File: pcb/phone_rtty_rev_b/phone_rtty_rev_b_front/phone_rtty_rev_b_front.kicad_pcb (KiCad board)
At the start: 2 copper layers, 58 x 24 mm, 3 parts

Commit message: Minor changes.
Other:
- outline, holes or cut-outs redrawn
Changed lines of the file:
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@@
       (xy -2.537313 2.939947) (xy -2.454562 2.96715) (xy -2.376928 2.977424) (xy -2.273043 2.973429)) (layer B.Cu) (width 0.01))
   )
-  (gr_circle (center 133.5 111.7) (end 137 111.7) (layer Edge.Cuts) (width 0.15))
-  (gr_circle (center 143.7 111.7) (end 147.2 111.7) (layer Edge.Cuts) (width 0.15))
-  (gr_line (start 122.7 110.4) (end 122.7 117.2) (angle 90) (layer Dwgs.User) (width 0.05))
+  (gr_arc (start 143.7 111.7) (end 140.8 114.6) (angle 90) (layer F.SilkS) (width 0.35))
+  (gr_arc (start 143.7 111.7) (end 140.8 108.8) (angle 90) (layer F.SilkS) (width 0.35))
+  (gr_arc (start 143.7 111.7) (end 146.6 108.8) (angle 90) (layer F.SilkS) (width 0.35))
+  (gr_arc (start 133.5 111.7) (end 130.6 114.6) (angle 90) (layer F.SilkS) (width 0.35))
+  (gr_arc (start 133.5 111.7) (end 130.6 108.8) (angle 90) (layer F.SilkS) (width 0.35))
+  (gr_arc (start 133.5 111.7) (end 136.4 108.8) (angle 90) (layer F.SilkS) (width 0.35))
+  (gr_circle (center 122.7 114.2) (end 122.7 117.1) (layer Edge.Cuts) (width 0.15))
+  (gr_line (start 122.7 110.8) (end 122.7 117.6) (angle 90) (layer Dwgs.User) (width 0.05))
+  (gr_circle (center 133.5 111.7) (end 136.5 111.7) (layer Edge.Cuts) (width 0.15))
+  (gr_circle (center 143.7 111.7) (end 146.7 111.7) (layer Edge.Cuts) (width 0.15))
   (gr_line (start 140.5 108.5) (end 140.2 108.2) (angle 90) (layer F.SilkS) (width 0.35))
-  (gr_arc (start 143.7 111.7) (end 146.9 108.5) (angle 90) (layer F.SilkS) (width 0.35))
-  (gr_arc (start 143.7 111.7) (end 140.5 108.5) (angle 90) (layer F.SilkS) (width 0.35))
-  (gr_arc (start 143.7 111.7) (end 140.5 114.9) (angle 90) (layer F.SilkS) (width 0.35))
-  (gr_arc (start 133.5 111.7) (end 136.7 108.5) (angle 90) (layer F.SilkS) (width 0.35))
-  (gr_arc (start 133.5 111.7) (end 130.3 108.5) (angle 90) (layer F.SilkS) (width 0.35))
-  (gr_arc (start 133.5 111.7) (end 130.3 114.9) (angle 90) (layer F.SilkS) (width 0.35))
   (gr_line (start 147.2 115.2) (end 140.3 108.3) (angle 90) (layer Dwgs.User) (width 0.05))
   (gr_line (start 140.2 115.2) (end 147.2 108.2) (angle 90) (layer Dwgs.User) (width 0.05))
@@
   (gr_line (start 130 108.2) (end 130.3 108.5) (angle 90) (layer F.SilkS) (width 0.35))
   (gr_line (start 137 108.2) (end 136.7 108.5) (angle 90) (layer F.SilkS) (width 0.35))
-  (gr_line (start 128.5 111.7) (end 128.95 111.7) (angle 90) (layer F.SilkS) (width 0.35))
-  (gr_line (start 133.5 106.7) (end 133.5 107.15) (angle 90) (layer F.SilkS) (width 0.35))
-  (gr_line (start 118.8 113.8) (end 126.6 113.8) (angle 90) (layer Dwgs.User) (width 0.05))
+  (gr_line (start 128.55 111.7) (end 129 111.7) (angle 90) (layer F.SilkS) (width 0.35))
+  (gr_line (start 133.5 106.75) (end 133.5 107.2) (angle 90) (layer F.SilkS) (width 0.35))
+  (gr_line (start 118.8 114.2) (end 126.6 114.2) (angle 90) (layer Dwgs.User) (width 0.05))
   (gr_text "PCB level" (at 152.4 115.9) (layer Cmts.User)
     (effects (font (size 1.2 1.2) (thickness 0.1)))
@@
     (arrow2b (pts (xy 92 111.7) (xy 92.586421 112.826504)))
   )
-  (gr_line (start 138.05 111.7) (end 138.4 111.7) (angle 90) (layer F.SilkS) (width 0.35))
-  (gr_line (start 138.8 111.7) (end 139.15 111.7) (angle 90) (layer F.SilkS) (width 0.35))
-  (gr_line (start 148.25 111.7) (end 148.7 111.7) (angle 90) (layer F.SilkS) (width 0.35))
-  (gr_line (start 143.7 107.15) (end 143.7 106.7) (angle 90) (layer F.SilkS) (width 0.35))
+  (gr_line (start 138 111.7) (end 138.35 111.7) (angle 90) (layer F.SilkS) (width 0.35))
+  (gr_line (start 138.85 111.7) (end 139.2 111.7) (angle 90) (layer F.SilkS) (width 0.35))
+  (gr_line (start 148.2 111.7) (end 148.65 111.7) (angle 90) (layer F.SilkS) (width 0.35))
+  (gr_line (start 143.7 107.2) (end 143.7 106.75) (angle 90) (layer F.SilkS) (width 0.35))
   (gr_text PHONE (at 122.7 119.5) (layer F.SilkS)
     (effects (font (size 1.5 1.5) (thickness 0.3)))
@@
   (gr_line (start 133.5 106.7) (end 133.5 116.7) (angle 90) (layer Dwgs.User) (width 0.05))
   (gr_line (start 127.5 111.7) (end 149.7 111.7) (angle 90) (layer Dwgs.User) (width 0.05))
-  (gr_circle (center 122.7 113.8) (end 125.6 113.7) (layer Edge.Cuts) (width 0.15))
   (dimension 10.2 (width 0.1) (layer Dwgs.User)
     (gr_text "10.200 mm" (at 94.65 118.9 270) (layer Dwgs.User)

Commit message: Minor changes to revision B and gerbers.
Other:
- board text added: "RTTY Interface Rev. B Front Panel"
- board text removed: "RTTY Interface Revision B Front Panel"
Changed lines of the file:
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@@
     (links 0)
     (no_connects 0)
-    (area 99.924999 99.924999 158.075001 124.075001)
+    (area 81.883333 87.8 164.986666 136.700001)
     (thickness 1.6)
     (drawings 57)
@@
     (visible_elements 7FFFFFFF)
     (pcbplotparams
-      (layerselection 0x010f0_80000001)
+      (layerselection 0x010e0_80000001)
       (usegerberextensions true)
       (excludeedgelayer true)
@@
       (drillshape 0)
       (scaleselection 1)
-      (outputdirectory D:/MyProjects/phone_rtty_interface/gerbers))
+      (outputdirectory gerbers))
   )
   (net 0 "")
@@
       (xy -2.537313 2.939947) (xy -2.454562 2.96715) (xy -2.376928 2.977424) (xy -2.273043 2.973429)) (layer B.Cu) (width 0.01))
   )
+  (gr_line (start 147.8 111.7) (end 148.2 111.7) (angle 90) (layer F.SilkS) (width 0.35))
   (gr_arc (start 143.7 111.7) (end 140.8 114.6) (angle 90) (layer F.SilkS) (width 0.35))
   (gr_arc (start 143.7 111.7) (end 140.8 108.8) (angle 90) (layer F.SilkS) (width 0.35))
@@
   (gr_circle (center 133.5 111.7) (end 136.5 111.7) (layer Edge.Cuts) (width 0.15))
   (gr_circle (center 143.7 111.7) (end 146.7 111.7) (layer Edge.Cuts) (width 0.15))
-  (gr_line (start 140.5 108.5) (end 140.2 108.2) (angle 90) (layer F.SilkS) (width 0.35))
+  (gr_line (start 140.8 108.8) (end 140.5 108.5) (angle 90) (layer F.SilkS) (width 0.35))
   (gr_line (start 147.2 115.2) (end 140.3 108.3) (angle 90) (layer Dwgs.User) (width 0.05))
   (gr_line (start 140.2 115.2) (end 147.2 108.2) (angle 90) (layer Dwgs.User) (width 0.05))
   (gr_line (start 137 115.2) (end 130 108.2) (angle 90) (layer Dwgs.User) (width 0.05))
   (gr_line (start 130 115.2) (end 137 108.2) (angle 90) (layer Dwgs.User) (width 0.05))
-  (gr_line (start 147.2 115.2) (end 146.9 114.9) (angle 90) (layer F.SilkS) (width 0.35))
-  (gr_line (start 140.2 115.2) (end 140.5 114.9) (angle 90) (layer F.SilkS) (width 0.35))
-  (gr_line (start 147.2 108.2) (end 146.9 108.5) (angle 90) (layer F.SilkS) (width 0.35))
-  (gr_line (start 137 115.2) (end 136.7 114.9) (angle 90) (layer F.SilkS) (width 0.35))
-  (gr_line (start 130 115.2) (end 130.3 114.9) (angle 90) (layer F.SilkS) (width 0.35))
-  (gr_line (start 130 108.2) (end 130.3 108.5) (angle 90) (layer F.SilkS) (width 0.35))
-  (gr_line (start 137 108.2) (end 136.7 108.5) (angle 90) (layer F.SilkS) (width 0.35))
-  (gr_line (start 128.55 111.7) (end 129 111.7) (angle 90) (layer F.SilkS) (width 0.35))
-  (gr_line (start 133.5 106.75) (end 133.5 107.2) (angle 90) (layer F.SilkS) (width 0.35))
+  (gr_line (start 146.9 114.9) (end 146.6 114.6) (angle 90) (layer F.SilkS) (width 0.35))
+  (gr_line (start 140.5 114.9) (end 140.8 114.6) (angle 90) (layer F.SilkS) (width 0.35))
+  (gr_line (start 146.9 108.5) (end 146.6 108.8) (angle 90) (layer F.SilkS) (width 0.35))
+  (gr_line (start 136.7 114.9) (end 136.4 114.6) (angle 90) (layer F.SilkS) (width 0.35))
+  (gr_line (start 130.3 114.9) (end 130.6 114.6) (angle 90) (layer F.SilkS) (width 0.35))
+  (gr_line (start 130.3 108.5) (end 130.6 108.8) (angle 90) (layer F.SilkS) (width 0.35))
+  (gr_line (start 136.7 108.5) (end 136.4 108.8) (angle 90) (layer F.SilkS) (width 0.35))
+  (gr_line (start 129.05 111.7) (end 129.4 111.7) (angle 90) (layer F.SilkS) (width 0.35))
+  (gr_line (start 133.5 107.25) (end 133.5 107.6) (angle 90) (layer F.SilkS) (width 0.35))
   (gr_line (start 118.8 114.2) (end 126.6 114.2) (angle 90) (layer Dwgs.User) (width 0.05))
   (gr_text "PCB level" (at 152.4 115.9) (layer Cmts.User)
@@
     (arrow2b (pts (xy 92 111.7) (xy 92.586421 112.826504)))
   )
-  (gr_line (start 138 111.7) (end 138.35 111.7) (angle 90) (layer F.SilkS) (width 0.35))
-  (gr_line (start 138.85 111.7) (end 139.2 111.7) (angle 90) (layer F.SilkS) (width 0.35))
-  (gr_line (start 148.2 111.7) (end 148.65 111.7) (angle 90) (layer F.SilkS) (width 0.35))
-  (gr_line (start 143.7 107.2) (end 143.7 106.75) (angle 90) (layer F.SilkS) (width 0.35))
+  (gr_line (start 137.6 111.7) (end 137.95 111.7) (angle 90) (layer F.SilkS) (width 0.35))
+  (gr_line (start 139.25 111.7) (end 139.6 111.7) (angle 90) (layer F.SilkS) (width 0.35))
+  (gr_line (start 143.7 107.25) (end 143.7 107.6) (angle 90) (layer F.SilkS) (width 0.35))
   (gr_text PHONE (at 122.7 119.5) (layer F.SilkS)
     (effects (font (size 1.5 1.5) (thickness 0.3)))
@@
   (gr_line (start 104 124) (end 104 135) (angle 90) (layer Dwgs.User) (width 0.15))
   (gr_line (start 100 116.7) (end 158 116.7) (angle 90) (layer Dwgs.User) (width 0.05))
-  (gr_arc (start 101 101) (end 100 101) (angle 90) (layer Edge.Cuts) (width 0.15))
-  (gr_arc (start 101 123) (end 101 124) (angle 90) (layer Edge.Cuts) (width 0.15))
-  (gr_arc (start 157 123) (end 158 123) (angle 90) (layer Edge.Cuts) (width 0.15))
-  (gr_arc (start 157 101) (end 157 100) (angle 90) (layer Edge.Cuts) (width 0.15))
-  (gr_text "RTTY Interface\nRevision B\nFront Panel" (at 129 89) (layer Cmts.User)
+  (gr_arc (start 101 101) (end 100 101) (angle 90) (layer Edge.Cuts) (width 0.1))
+  (gr_arc (start 101 123) (end 101 124) (angle 90) (layer Edge.Cuts) (width 0.1))
+  (gr_arc (start 157 123) (end 158 123) (angle 90) (layer Edge.Cuts) (width 0.1))
+  (gr_arc (start 157 101) (end 157 100) (angle 90) (layer Edge.Cuts) (width 0.1))
+  (gr_text "RTTY Interface Rev. B\nFront Panel" (at 129 91) (layer Cmts.User)
     (effects (font (size 2 2) (thickness 0.3)))
   )
@@
     (effects (font (size 1.5 1.5) (thickness 0.25)))
   )
-  (gr_line (start 158 101) (end 158 123) (angle 90) (layer Edge.Cuts) (width 0.15))
-  (gr_line (start 100 101) (end 100 123) (angle 90) (layer Edge.Cuts) (width 0.15))
-  (gr_line (start 101 100) (end 157 100) (angle 90) (layer Edge.Cuts) (width 0.15))
-  (gr_line (start 101 124) (end 157 124) (angle 90) (layer Edge.Cuts) (width 0.15))
+  (gr_line (start 158 101) (end 158 123) (angle 90) (layer Edge.Cuts) (width 0.1))
+  (gr_line (start 100 101) (end 100 123) (angle 90) (layer Edge.Cuts) (width 0.1))
+  (gr_line (start 101 100) (end 157 100) (angle 90) (layer Edge.Cuts) (width 0.1))
+  (gr_line (start 101 124) (end 157 124) (angle 90) (layer Edge.Cuts) (width 0.1))
 )

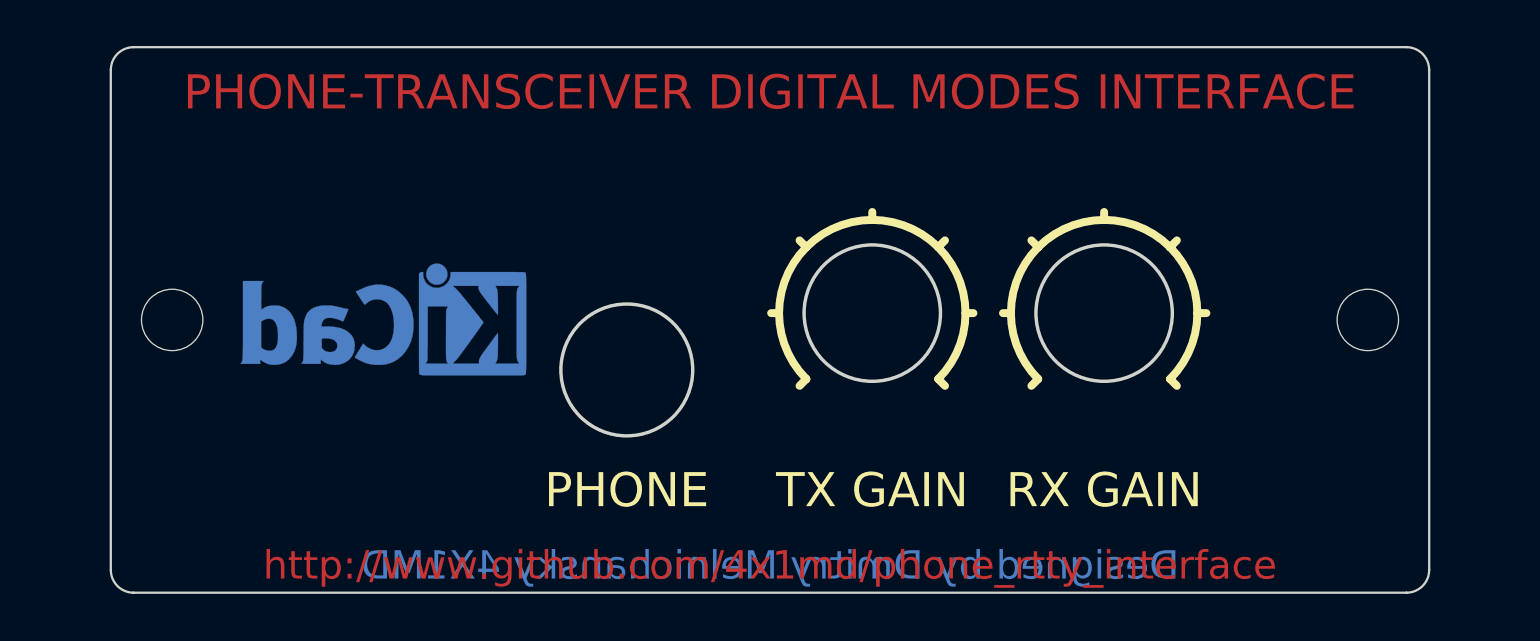
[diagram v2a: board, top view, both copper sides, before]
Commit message: Main board and panels corrections.
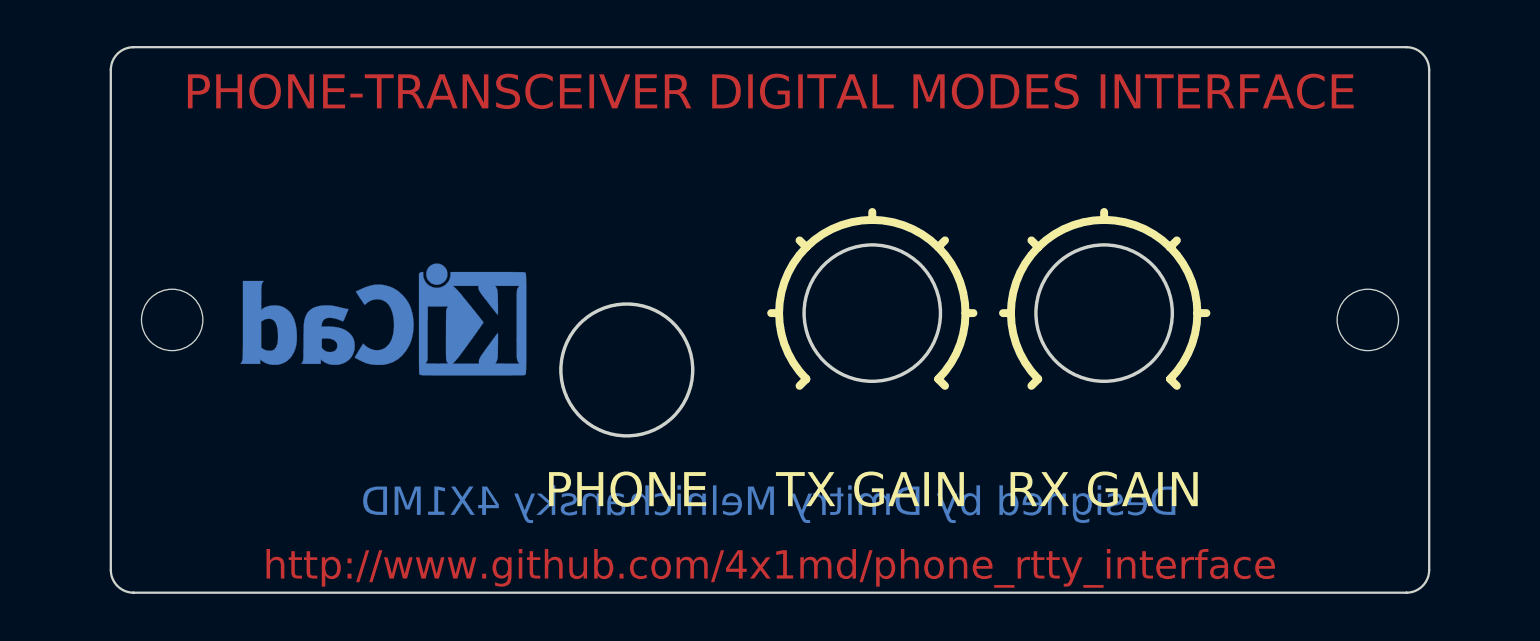
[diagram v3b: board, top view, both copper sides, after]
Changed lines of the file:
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@@
     (effects (font (size 2 2) (thickness 0.3)))
   )
-  (gr_text "Designed by Dmitry Melnichansky 4X1MD" (at 129 122.8) (layer B.Cu)
+  (gr_text "Designed by Dmitry Melnichansky 4X1MD" (at 129 120) (layer B.Cu)
     (effects (font (size 1.25 1.25) (thickness 0.2)) (justify mirror))
   )
